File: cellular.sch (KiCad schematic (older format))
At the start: 16 parts, among them J4 SIM_Card, U10 M26

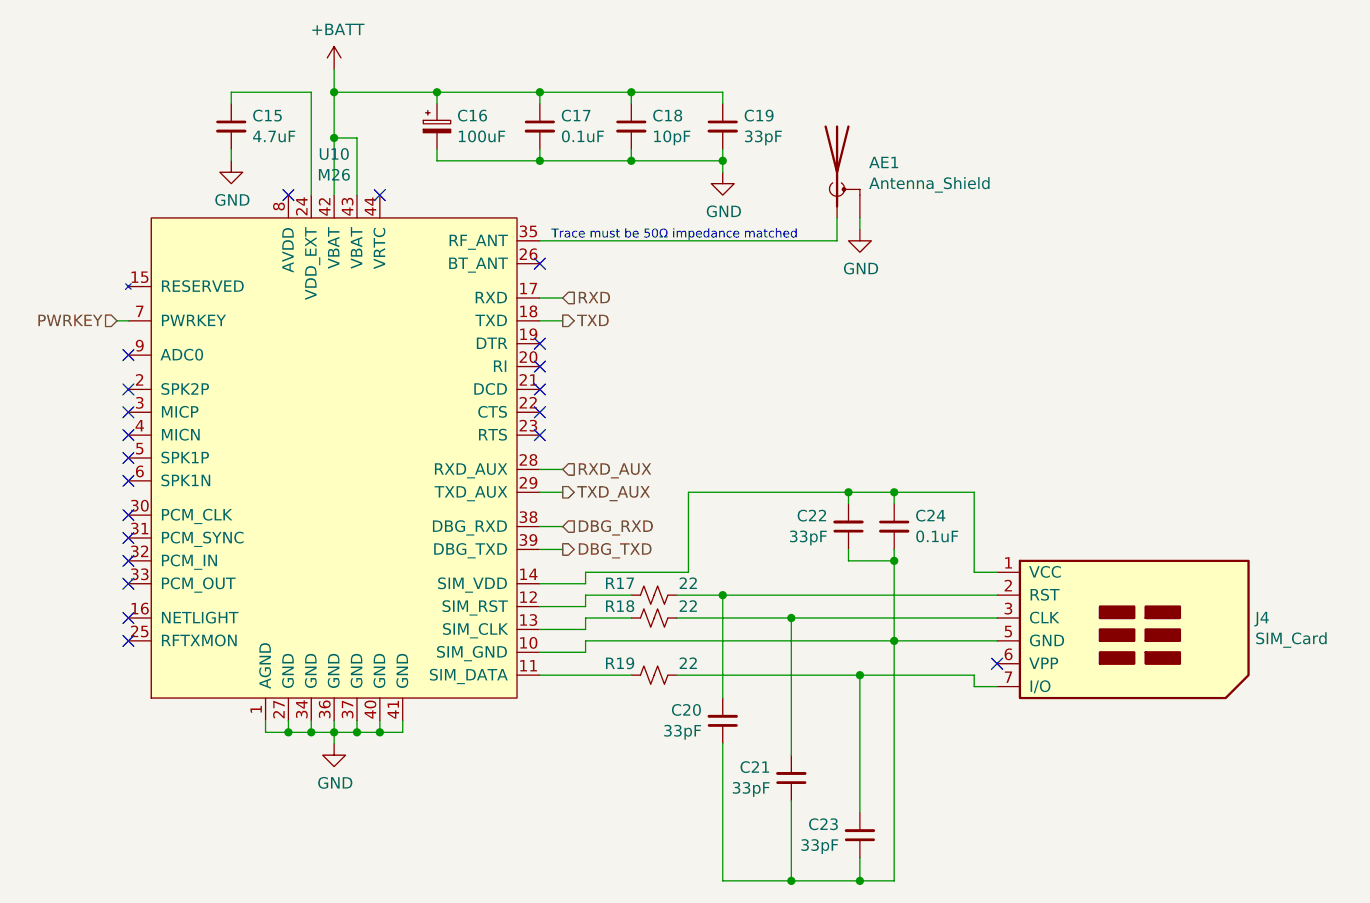
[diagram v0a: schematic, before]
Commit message: clear existing annotations from schematic
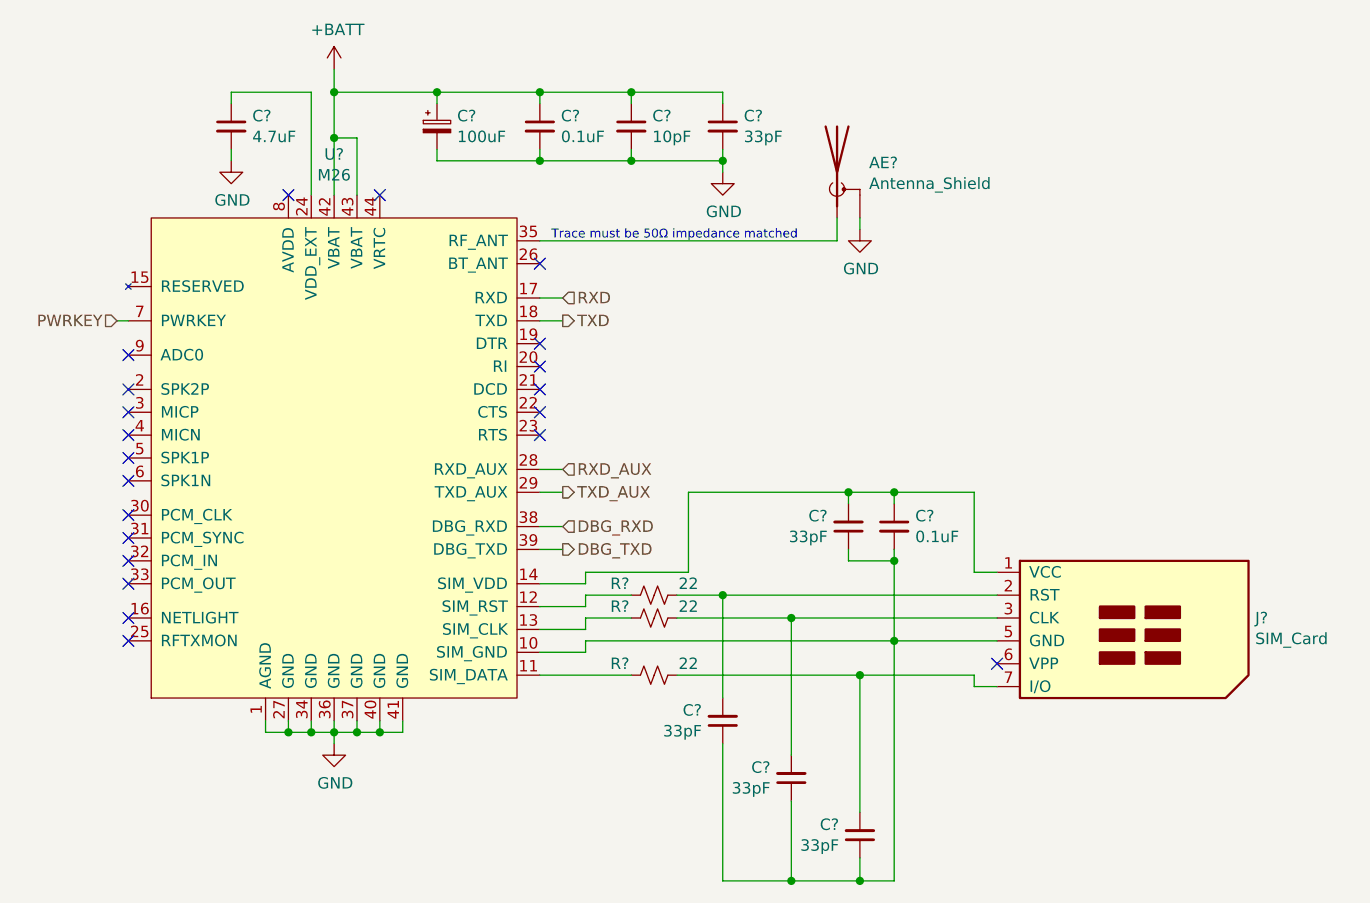
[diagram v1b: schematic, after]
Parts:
- renumbered AE1 to AE?, C15 to C?, C24 to C?, C22 to C?, C20 to C?, C21 to C?, C23 to C?, C16 to C?, C17 to C?, C18 to C?, C19 to C?, J4 to J?, R17 to R?, R18 to R?, R19 to R?, U10 to U?
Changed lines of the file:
@@
 $EndDescr
 $Comp
-L phone:M26 U10
+L phone:M26 U?
 U 1 1 5C9AECA6
 P 2250 2550
-F 0 "U10" H 2250 3878 50  0000 C CNN
+F 0 "U?" H 2250 3878 50  0000 C CNN
 F 1 "M26" H 2250 3787 50  0000 C CNN
 F 2 "phone:M26" H 2250 2550 50  0001 C CNN
@@
 NoConn ~ 1350 2650
 $Comp
-L Device:Antenna_Shield AE1
+L Device:Antenna_Shield AE?
 U 1 1 5C9AEE16
 P 4450 1300
-F 0 "AE1" H 4590 1341 50  0000 L CNN
+F 0 "AE?" H 4590 1341 50  0000 L CNN
 F 1 "Antenna_Shield" H 4590 1250 50  0000 L CNN
 F 2 "Connector_Coaxial:U.FL_Molex_MCRF_73412-0110_Vertical" H 4450 1400 50  0001 C CNN
@@
 	4450 1600 4450 1500
 $Comp
-L power:GND #PWR051
+L power:GND #PWR?
 U 1 1 5C9AEED4
 P 4550 1550
-F 0 "#PWR051" H 4550 1300 50  0001 C CNN
+F 0 "#PWR?" H 4550 1300 50  0001 C CNN
 F 1 "GND" H 4555 1377 50  0000 C CNN
 F 2 "" H 4550 1550 50  0001 C CNN
@@
 NoConn ~ 1350 3250
 $Comp
-L power:GND #PWR049
+L power:GND #PWR?
 U 1 1 5C9B042C
 P 2250 3800
-F 0 "#PWR049" H 2250 3550 50  0001 C CNN
+F 0 "#PWR?" H 2250 3550 50  0001 C CNN
 F 1 "GND" H 2255 3627 50  0000 C CNN
 F 2 "" H 2250 3800 50  0001 C CNN
@@
 	2250 3750 2250 3800
 $Comp
-L Connector:SIM_Card J4
+L Connector:SIM_Card J?
 U 1 1 5C9B0C92
 P 5650 3350
-F 0 "J4" H 6279 3450 50  0000 L CNN
+F 0 "J?" H 6279 3450 50  0000 L CNN
 F 1 "SIM_Card" H 6279 3359 50  0000 L CNN
 F 2 "phone:7112S0815X19LF" H 5650 3700 50  0001 C CNN
@@
 	2350 1150 2250 1150
 $Comp
-L power:+BATT #PWR048
+L power:+BATT #PWR?
 U 1 1 5CA67C60
 P 2250 850
-F 0 "#PWR048" H 2250 700 50  0001 C CNN
+F 0 "#PWR?" H 2250 700 50  0001 C CNN
 F 1 "+BATT" H 2265 1023 50  0000 C CNN
 F 2 "" H 2250 850 50  0001 C CNN
@@
 NoConn ~ 2050 1400
 $Comp
-L Device:C_Small C15
+L Device:C_Small C?
 U 1 1 5D5D7303
 P 1800 1100
-F 0 "C15" H 1892 1146 50  0000 L CNN
+F 0 "C?" H 1892 1146 50  0000 L CNN
 F 1 "4.7uF" H 1892 1055 50  0000 L CNN
 F 2 "Capacitor_SMD:C_0603_1608Metric_Pad1.05x0.95mm_HandSolder" H 1800 1100 50  0001 C CNN
@@
 $EndComp
 $Comp
-L power:GND #PWR047
+L power:GND #PWR?
 U 1 1 5D5D9D65
 P 1800 1250
-F 0 "#PWR047" H 1800 1000 50  0001 C CNN
+F 0 "#PWR?" H 1800 1000 50  0001 C CNN
 F 1 "GND" H 1805 1077 50  0000 C CNN
 F 2 "" H 1800 1250 50  0001 C CNN
@@
 	1800 950  1800 1000
 $Comp
-L Device:C_Small C24
+L Device:C_Small C?
 U 1 1 5D5DD206
 P 4700 2850
-F 0 "C24" H 4792 2896 50  0000 L CNN
+F 0 "C?" H 4792 2896 50  0000 L CNN
 F 1 "0.1uF" H 4792 2805 50  0000 L CNN
 F 2 "Capacitor_SMD:C_0603_1608Metric_Pad1.05x0.95mm_HandSolder" H 4700 2850 50  0001 C CNN
@@
 NoConn ~ 5150 3450
 $Comp
-L Device:R_Small_US R17
+L Device:R_Small_US R?
 U 1 1 5D5E2ECB
 P 3650 3150
-F 0 "R17" V 3600 3000 50  0000 C CNN
+F 0 "R?" V 3600 3000 50  0000 C CNN
 F 1 "22" V 3600 3300 50  0000 C CNN
 F 2 "Resistor_SMD:R_0603_1608Metric_Pad1.05x0.95mm_HandSolder" H 3650 3150 50  0001 C CNN
@@
 	3750 3150 3950 3150
 $Comp
-L Device:R_Small_US R18
+L Device:R_Small_US R?
 U 1 1 5D5E8317
 P 3650 3250
-F 0 "R18" V 3600 3100 50  0000 C CNN
+F 0 "R?" V 3600 3100 50  0000 C CNN
 F 1 "22" V 3600 3400 50  0000 C CNN
 F 2 "Resistor_SMD:R_0603_1608Metric_Pad1.05x0.95mm_HandSolder" H 3650 3250 50  0001 C CNN
@@
 Connection ~ 4700 2700
 $Comp
-L Device:R_Small_US R19
+L Device:R_Small_US R?
 U 1 1 5D5F3F1B
 P 3650 3500
-F 0 "R19" V 3600 3350 50  0000 C CNN
+F 0 "R?" V 3600 3350 50  0000 C CNN
 F 1 "22" V 3600 3650 50  0000 C CNN
 F 2 "Resistor_SMD:R_0603_1608Metric_Pad1.05x0.95mm_HandSolder" H 3650 3500 50  0001 C CNN
@@
 	5050 3500 4550 3500
 $Comp
-L Device:C_Small C22
+L Device:C_Small C?
 U 1 1 5D5F7DFB
 P 4500 2850
-F 0 "C22" H 4409 2804 50  0000 R CNN
+F 0 "C?" H 4409 2804 50  0000 R CNN
 F 1 "33pF" H 4409 2895 50  0000 R CNN
 F 2 "Capacitor_SMD:C_0603_1608Metric_Pad1.05x0.95mm_HandSolder" H 4500 2850 50  0001 C CNN
@@
 	4500 2700 4700 2700
 $Comp
-L Device:C_Small C20
+L Device:C_Small C?
 U 1 1 5D5FC3FC
 P 3950 3700
-F 0 "C20" H 3859 3654 50  0000 R CNN
+F 0 "C?" H 3859 3654 50  0000 R CNN
 F 1 "33pF" H 3859 3745 50  0000 R CNN
 F 2 "Capacitor_SMD:C_0603_1608Metric_Pad1.05x0.95mm_HandSolder" H 3950 3700 50  0001 C CNN
@@
 	3950 3150 5150 3150
 $Comp
-L Device:C_Small C21
+L Device:C_Small C?
 U 1 1 5D5FDAEC
 P 4250 3950
-F 0 "C21" H 4159 3904 50  0000 R CNN
+F 0 "C?" H 4159 3904 50  0000 R CNN
 F 1 "33pF" H 4159 3995 50  0000 R CNN
 F 2 "Capacitor_SMD:C_0603_1608Metric_Pad1.05x0.95mm_HandSolder" H 4250 3950 50  0001 C CNN
@@
 	3150 3500 3550 3500
 $Comp
-L Device:C_Small C23
+L Device:C_Small C?
 U 1 1 5D60FB3C
 P 4550 4200
-F 0 "C23" H 4459 4154 50  0000 R CNN
+F 0 "C?" H 4459 4154 50  0000 R CNN
 F 1 "33pF" H 4459 4245 50  0000 R CNN
 F 2 "Capacitor_SMD:C_0603_1608Metric_Pad1.05x0.95mm_HandSolder" H 4550 4200 50  0001 C CNN
@@
 Connection ~ 4250 4400
 $Comp
-L Device:CP_Small C16
+L Device:CP_Small C?
 U 1 1 5D622E7F
 P 2700 1100
-F 0 "C16" H 2788 1146 50  0000 L CNN
+F 0 "C?" H 2788 1146 50  0000 L CNN
 F 1 "100uF" H 2788 1055 50  0000 L CNN
 F 2 "Capacitor_Tantalum_SMD:CP_EIA-3528-15_AVX-H_Pad1.50x2.35mm_HandSolder" H 2700 1100 50  0001 C CNN
@@
 $EndComp
 $Comp
-L Device:C_Small C17
+L Device:C_Small C?
 U 1 1 5D623741
 P 3150 1100
-F 0 "C17" H 3242 1146 50  0000 L CNN
+F 0 "C?" H 3242 1146 50  0000 L CNN
 F 1 "0.1uF" H 3242 1055 50  0000 L CNN
 F 2 "Capacitor_SMD:C_0603_1608Metric_Pad1.05x0.95mm_HandSolder" H 3150 1100 50  0001 C CNN
@@
 $EndComp
 $Comp
-L Device:C_Small C18
+L Device:C_Small C?
 U 1 1 5D626C11
 P 3550 1100
-F 0 "C18" H 3642 1146 50  0000 L CNN
+F 0 "C?" H 3642 1146 50  0000 L CNN
 F 1 "10pF" H 3642 1055 50  0000 L CNN
 F 2 "Capacitor_SMD:C_0603_1608Metric_Pad1.05x0.95mm_HandSolder" H 3550 1100 50  0001 C CNN
@@
 $EndComp
 $Comp
-L Device:C_Small C19
+L Device:C_Small C?
 U 1 1 5D627055
 P 3950 1100
-F 0 "C19" H 4042 1146 50  0000 L CNN
+F 0 "C?" H 4042 1146 50  0000 L CNN
 F 1 "33pF" H 4042 1055 50  0000 L CNN
 F 2 "Capacitor_SMD:C_0603_1608Metric_Pad1.05x0.95mm_HandSolder" H 3950 1100 50  0001 C CNN
@@
 	3550 1250 3150 1250
 $Comp
-L power:GND #PWR050
+L power:GND #PWR?
 U 1 1 5D634214
 P 3950 1300
-F 0 "#PWR050" H 3950 1050 50  0001 C CNN
+F 0 "#PWR?" H 3950 1050 50  0001 C CNN
 F 1 "GND" H 3955 1127 50  0000 C CNN
 F 2 "" H 3950 1300 50  0001 C CNN

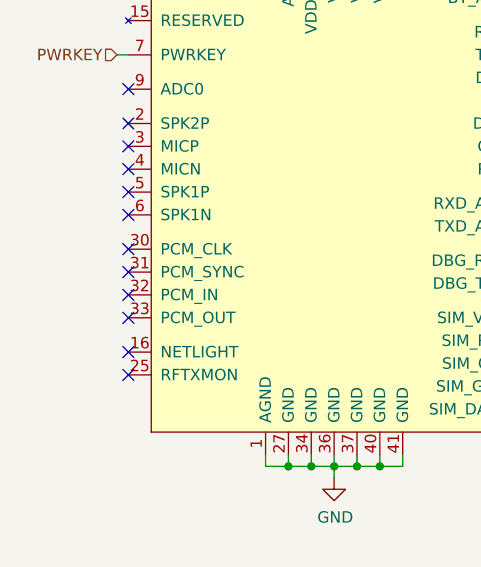
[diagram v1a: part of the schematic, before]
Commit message: add buttons and connect pcm interface of modem to esp32
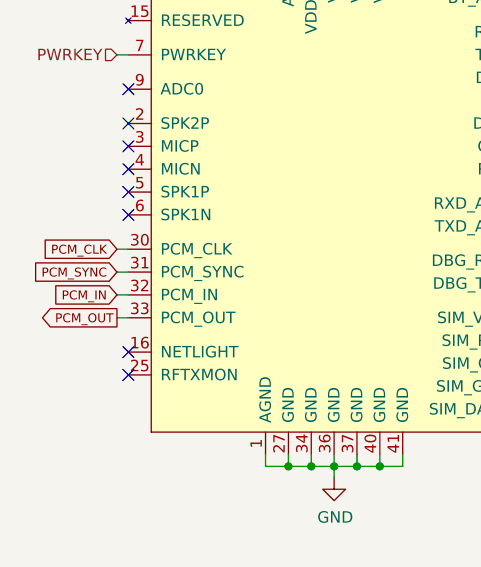
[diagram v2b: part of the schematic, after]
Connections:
- net PCM_CLK: now reaches U?.30 (PCM_CLK)
- net PCM_SYNC: now reaches U?.31 (PCM_SYNC)
- net PCM_IN: now reaches U?.32 (PCM_IN)
- net PCM_OUT: now reaches U?.33 (PCM_OUT)
- no-connect marks 21 -> 17
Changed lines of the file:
@@
 Wire Wire Line
 	3150 1600 4450 1600
-NoConn ~ 1350 2800
-NoConn ~ 1350 2900
-NoConn ~ 1350 3000
-NoConn ~ 1350 3100
 NoConn ~ 1350 3350
 NoConn ~ 1350 3250
@@
 Connection ~ 3950 1250
 NoConn ~ 1350 2100
+Text GLabel 1300 2800 0    39   Input ~ 0
+PCM_CLK
+Text GLabel 1300 2900 0    39   Input ~ 0
+PCM_SYNC
+Text GLabel 1300 3000 0    39   Input ~ 0
+PCM_IN
+Text GLabel 1300 3100 0    39   Output ~ 0
+PCM_OUT
+Wire Wire Line
+	1300 2800 1350 2800
+Wire Wire Line
+	1350 2900 1300 2900
+Wire Wire Line
+	1300 3000 1350 3000
+Wire Wire Line
+	1350 3100 1300 3100
 $EndSCHEMATC

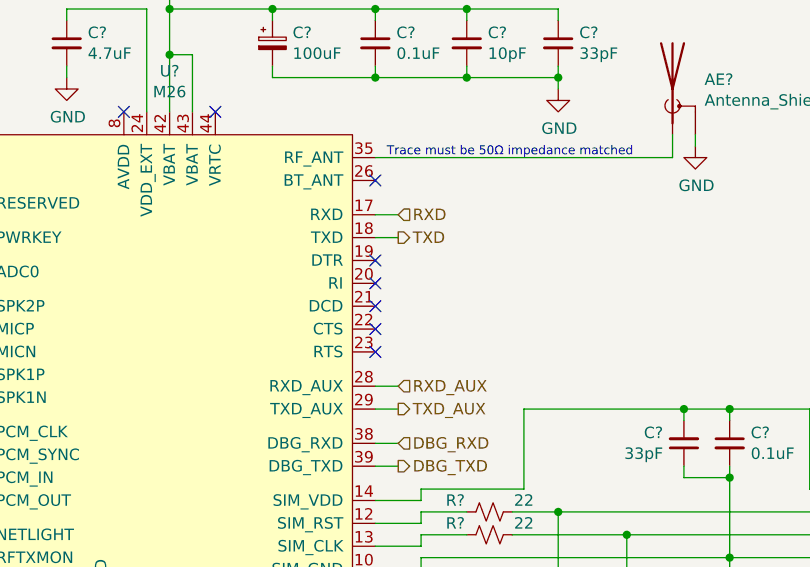
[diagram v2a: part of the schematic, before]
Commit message: connect RI to esp32
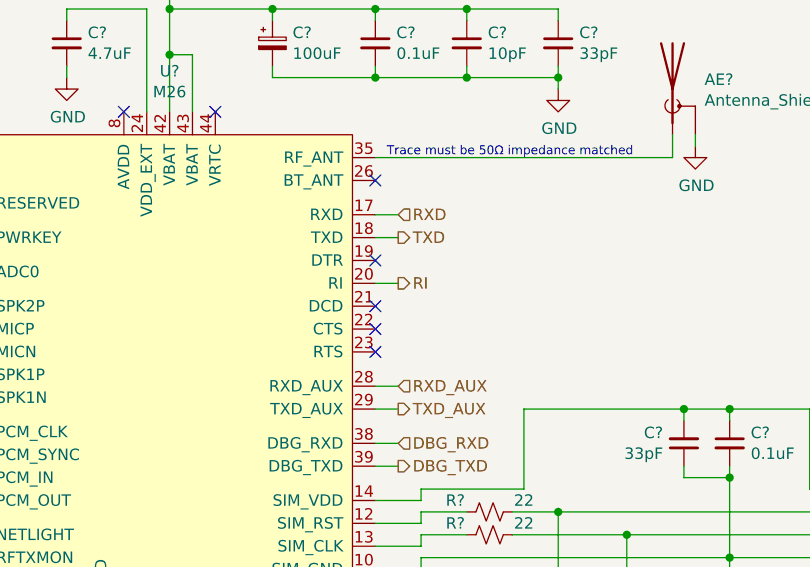
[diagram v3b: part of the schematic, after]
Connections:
- net RI: now reaches U?.20 (RI)
- no-connect marks 17 -> 16
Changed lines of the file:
@@
 TXD
 NoConn ~ 3150 2050
-NoConn ~ 3150 2150
 NoConn ~ 3150 2250
 NoConn ~ 3150 2350
@@
 Wire Wire Line
 	1350 3100 1300 3100
+Text HLabel 3250 2150 2    50   Output ~ 0
+RI
+Wire Wire Line
+	3150 2150 3250 2150
 $EndSCHEMATC
